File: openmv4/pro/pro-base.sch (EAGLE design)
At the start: 172 parts, among them J2 SAMTEC_FTSH-105-01-F-DVSAMTEC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, J6 RSP-122811-01, M1 9774030243R, M2 9774030243R, Q1 BSS138, Q2 AO3401, U1 W25Q256JVEIQ_TR, U10 STM32H743IIK6, U11 TEXAS_INSTRUMENTS_BQ24072TRGT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, U12 MICROCHIP_ATECC608A-SSHDA-BMI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, U14 IS42S32800, U2 EMIF06-MSD02N16, U3 ME6211C18M5G, U4 PAM2305AABADJ, U5 LSM6DS3TR-C, U6 MICROCHIP_USB3320C-EZK-TRMICR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, U7 LBEE5KL1DX-TEMP, U9 VL53L5CX, X2 USD-1040310811, X3 DF12-36-DS, X4 S2B-PH-K-S(LF)(SN), Y0 SITIME_SIT1533AI-H4-DCC-32.76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, Y1 DSC1001BI1-024.0000

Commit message: Update pro schematics
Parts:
- added D26: GREEN, SparkFun-LED:LED-GREEN0603
- added JP3, JP4: JUMPER-SMT_2_NC_PASTE_SILK, SparkFun-Jumpers:JUMPER-SMT_2_NC_PASTE_SILK
- added R46: 1.5K, sfe:RESISTOR0402-RES
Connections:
- new net N$1: D26.A, R46.1
- new net N$11: JP4.1, R33.2
- new net N$12: JP3.1, R46.2
- new net N$9: D26.C, U11.!PGOOD!
- net OUT: now also JP3.2, JP4.2; no longer R33.2
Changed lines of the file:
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@@
 <part name="R45" library="sfe" deviceset="RESISTOR" device="0402-RES" value="46.4K"/>
 <part name="J6" library="RSP-122811-01" deviceset="RSP-122811-01" device=""/>
+<part name="R46" library="sfe" deviceset="RESISTOR" device="0402-RES" value="1.5K"/>
+<part name="D26" library="SparkFun-LED" library_urn="urn:adsk.eagle:library:529" deviceset="LED-GREEN" device="0603" package3d_urn="urn:adsk.eagle:package:39354/1" value="GREEN"/>
+<part name="JP3" library="SparkFun-Jumpers" library_urn="urn:adsk.eagle:library:528" deviceset="JUMPER-SMT_2_NC_PASTE" device="_SILK" package3d_urn="urn:adsk.eagle:package:39282/1"/>
+<part name="JP4" library="SparkFun-Jumpers" library_urn="urn:adsk.eagle:library:528" deviceset="JUMPER-SMT_2_NC_PASTE" device="_SILK" package3d_urn="urn:adsk.eagle:package:39282/1"/>
 </parts>
 <sheets>
@@
 <text x="96.52" y="391.16" size="1.27" layer="150" font="vector" ratio="20">* Swapped to make
   layout easier</text>
-<text x="134.62" y="358.14" size="7.62" layer="94" font="vector" ratio="20">Battery Charging</text>
+<text x="134.62" y="360.68" size="7.62" layer="94" font="vector" ratio="20">Battery Charging</text>
 <wire x1="132.08" y1="370.84" x2="271.78" y2="370.84" width="0.1524" layer="94" style="longdash"/>
 <text x="134.62" y="419.1" size="7.62" layer="94" font="vector" ratio="20">Power</text>
@@
 <attribute name="VALUE" x="407.924" y="92.202" size="1.778" layer="96" rot="MR0"/>
 </instance>
+<instance part="R46" gate="G$1" x="165.1" y="355.6" smashed="yes">
+<attribute name="NAME" x="161.29" y="357.0986" size="1.778" layer="95"/>
+<attribute name="VALUE" x="161.29" y="352.298" size="1.778" layer="96"/>
+</instance>
+<instance part="D26" gate="G$1" x="154.94" y="355.6" smashed="yes" rot="R270">
+<attribute name="NAME" x="150.368" y="359.029" size="1.778" layer="95" font="vector"/>
+<attribute name="VALUE" x="150.368" y="353.695" size="1.778" layer="96" font="vector" align="top-left"/>
+</instance>
+<instance part="JP3" gate="G$1" x="177.8" y="355.6" smashed="yes">
+<attribute name="NAME" x="175.26" y="358.14" size="1.778" layer="95" font="vector"/>
+<attribute name="VALUE" x="180.34" y="360.68" size="1.778" layer="96" font="vector" align="top-left"/>
+</instance>
+<instance part="JP4" gate="G$1" x="177.8" y="350.52" smashed="yes">
+<attribute name="NAME" x="175.26" y="353.06" size="1.778" layer="95" font="vector"/>
+<attribute name="VALUE" x="180.34" y="355.6" size="1.778" layer="96" font="vector" align="top-left"/>
+</instance>
 </instances>
 <busses>
@@
 <wire x1="193.04" y1="337.82" x2="215.9" y2="337.82" width="0.1524" layer="91"/>
 <junction x="193.04" y="337.82"/>
-<wire x1="193.04" y1="350.52" x2="193.04" y2="345.44" width="0.1524" layer="91"/>
 <pinref part="C4" gate="G$1" pin="2"/>
 <wire x1="193.04" y1="345.44" x2="193.04" y2="337.82" width="0.1524" layer="91"/>
 <wire x1="215.9" y1="337.82" x2="241.3" y2="337.82" width="0.1524" layer="91"/>
 <junction x="215.9" y="337.82"/>
-<pinref part="R33" gate="G$1" pin="2"/>
-<wire x1="193.04" y1="350.52" x2="170.18" y2="350.52" width="0.1524" layer="91"/>
 <pinref part="U11" gate="G$0" pin="EN2"/>
 <wire x1="165.1" y1="322.58" x2="162.56" y2="322.58" width="0.1524" layer="91"/>
@@
 <wire x1="162.56" y1="345.44" x2="193.04" y2="345.44" width="0.1524" layer="91"/>
 <junction x="193.04" y="345.44"/>
+<wire x1="193.04" y1="355.6" x2="193.04" y2="350.52" width="0.1524" layer="91"/>
+<pinref part="JP3" gate="G$1" pin="2"/>
+<wire x1="193.04" y1="350.52" x2="193.04" y2="345.44" width="0.1524" layer="91"/>
+<wire x1="182.88" y1="355.6" x2="193.04" y2="355.6" width="0.1524" layer="91"/>
+<pinref part="JP4" gate="G$1" pin="2"/>
+<wire x1="182.88" y1="350.52" x2="193.04" y2="350.52" width="0.1524" layer="91"/>
+<junction x="193.04" y="350.52"/>
 </segment>
 </net>
@@
 </segment>
 </net>
+<net name="N$1" class="0">
+<segment>
+<pinref part="D26" gate="G$1" pin="A"/>
+<pinref part="R46" gate="G$1" pin="1"/>
+<wire x1="157.48" y1="355.6" x2="160.02" y2="355.6" width="0.1524" layer="91"/>
+</segment>
+</net>
+<net name="N$9" class="0">
+<segment>
+<pinref part="D26" gate="G$1" pin="C"/>
+<wire x1="149.86" y1="355.6" x2="142.24" y2="355.6" width="0.1524" layer="91"/>
+<wire x1="142.24" y1="355.6" x2="142.24" y2="307.34" width="0.1524" layer="91"/>
+<pinref part="U11" gate="G$0" pin="!PGOOD!"/>
+<wire x1="142.24" y1="307.34" x2="165.1" y2="307.34" width="0.1524" layer="91"/>
+</segment>
+</net>
+<net name="N$11" class="0">
+<segment>
+<pinref part="R33" gate="G$1" pin="2"/>
+<pinref part="JP4" gate="G$1" pin="1"/>
+<wire x1="170.18" y1="350.52" x2="172.72" y2="350.52" width="0.1524" layer="91"/>
+</segment>
+</net>
+<net name="N$12" class="0">
+<segment>
+<pinref part="R46" gate="G$1" pin="2"/>
+<pinref part="JP3" gate="G$1" pin="1"/>
+<wire x1="170.18" y1="355.6" x2="172.72" y2="355.6" width="0.1524" layer="91"/>
+</segment>
+</net>

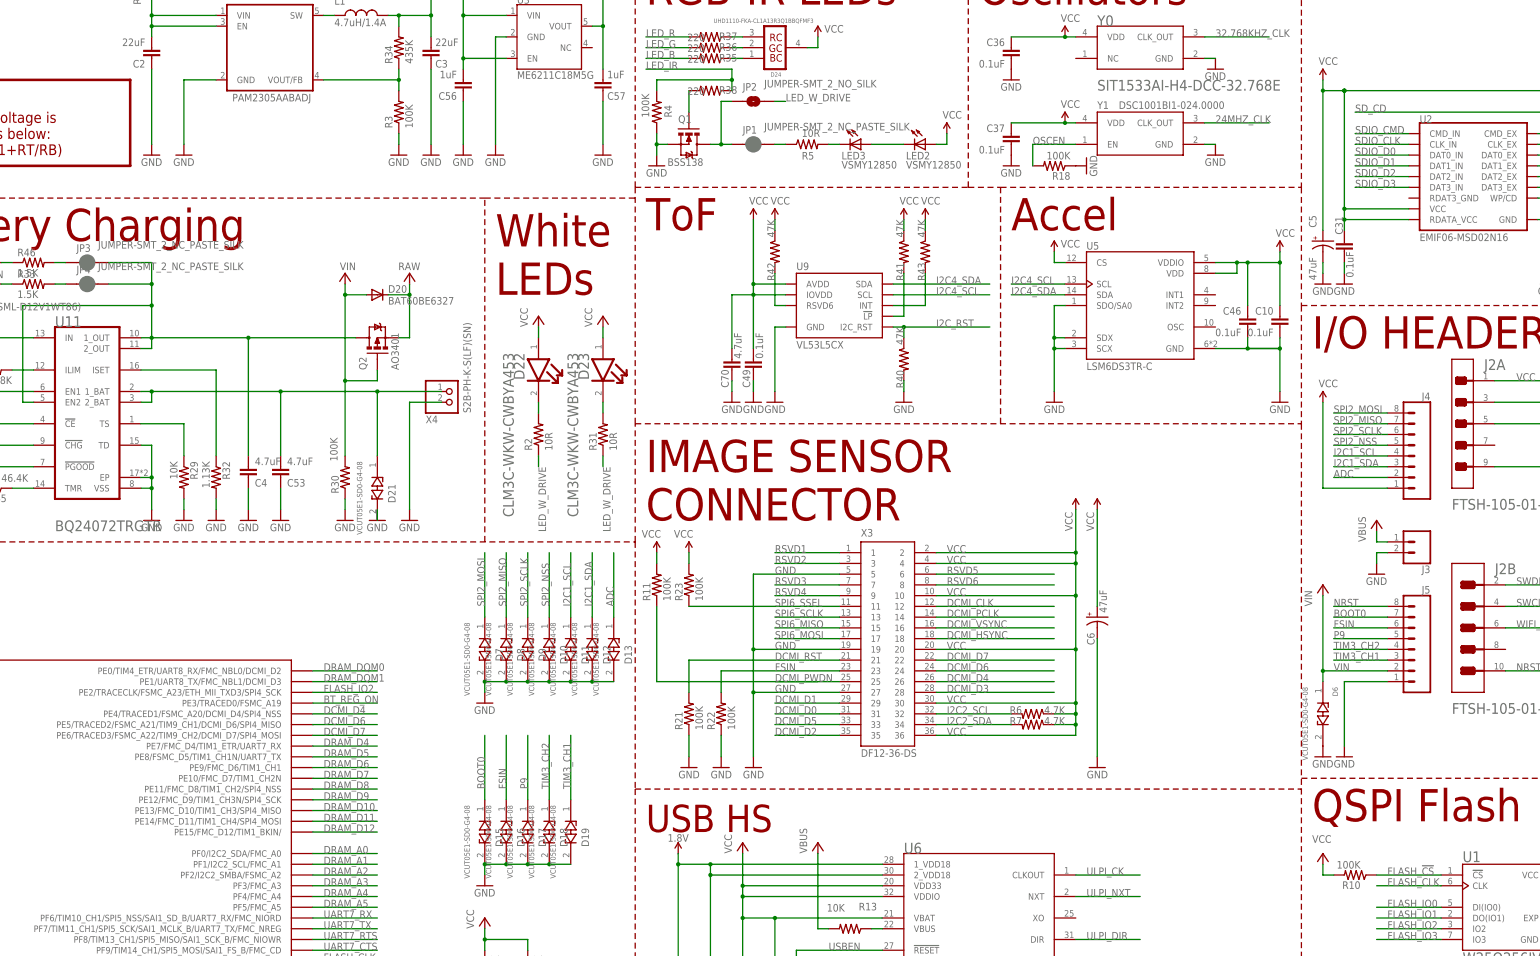
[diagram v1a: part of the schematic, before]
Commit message: Update jumpers to 0 ohm
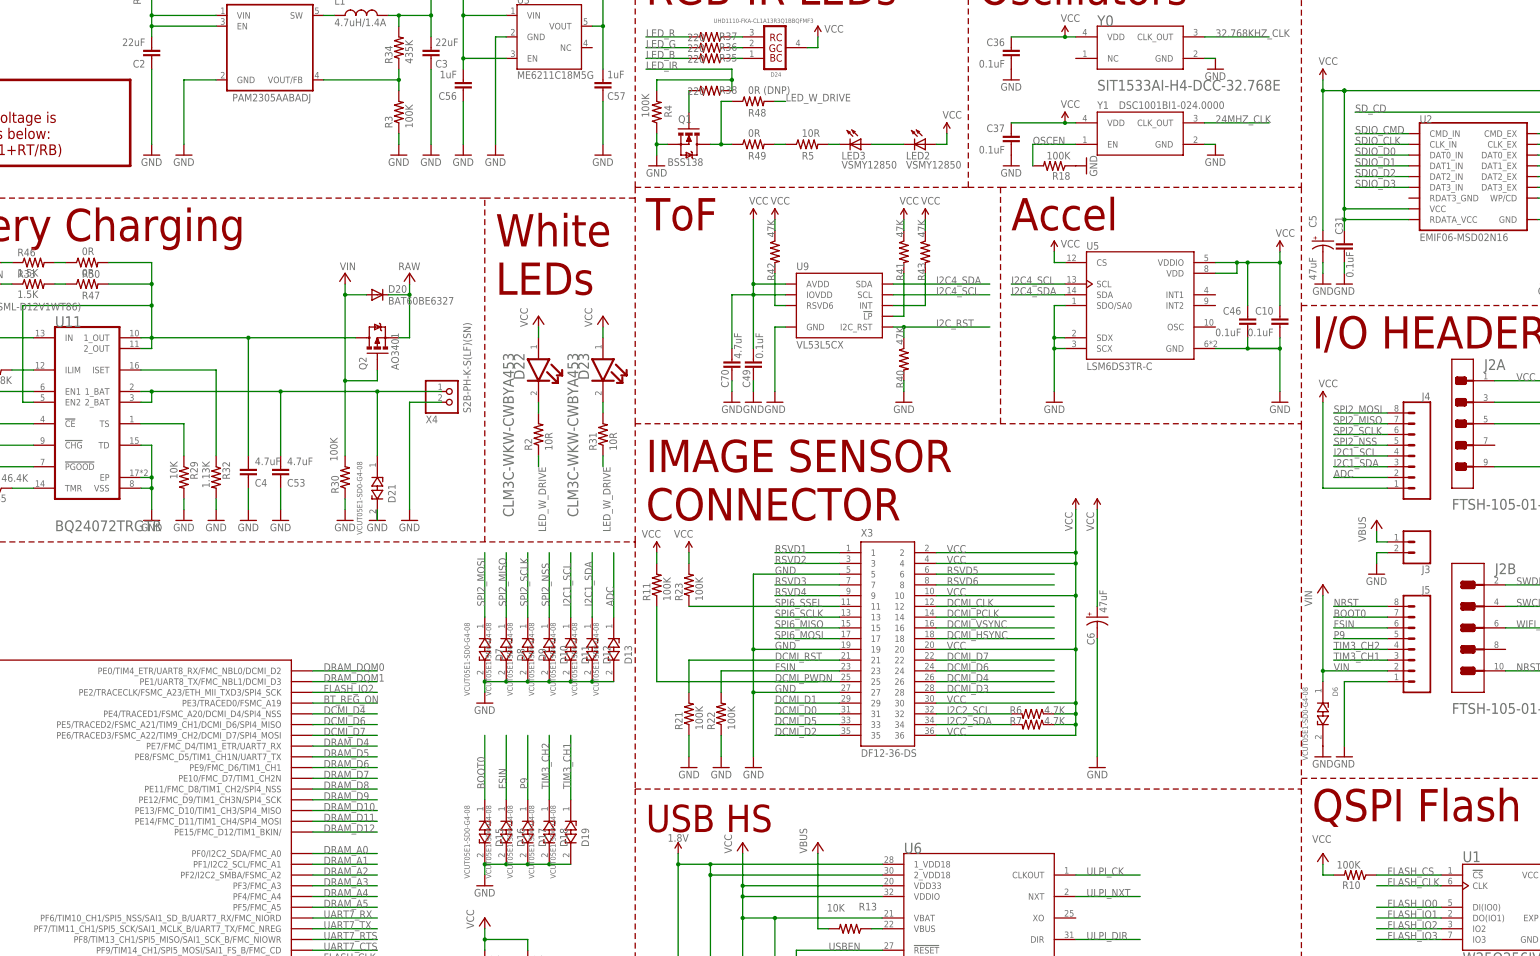
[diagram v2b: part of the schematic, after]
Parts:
- removed JP1, JP3, JP4: JUMPER-SMT_2_NC_PASTE_SILK, SparkFun-Jumpers:JUMPER-SMT_2_NC_PASTE_SILK
- removed JP2: JUMPER-SMT_2_NO_SILK, SparkFun-Jumpers:JUMPER-SMT_2_NO_SILK
- added R47, R49, R50: 0R, sfe:RESISTOR0402-RES
- added R48: 0R (DNP), sfe:RESISTOR0402-RES
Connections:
- removed net FLASH_!CS: R10.1, U1.!CS
- net FLASH_CS: now also R10.1, U1.!CS
- net LED_DRAIN: now also R48.1, R49.1; no longer JP1.1, JP2.1
- net LED_IR_DRIVE: now also R49.2; no longer JP1.2
- net LED_W_DRIVE: now also R48.2; no longer JP2.2
- net N$11: now also R47.1; no longer JP4.1
- net N$12: now also R50.1; no longer JP3.1
- net OUT: now also R47.2, R50.2; no longer JP3.2, JP4.2
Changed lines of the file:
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@@
 <part name="R2" library="sfe" deviceset="RESISTOR" device="0402-RES" value="10R"/>
 <part name="R31" library="sfe" deviceset="RESISTOR" device="0402-RES" value="10R"/>
-<part name="JP1" library="SparkFun-Jumpers" library_urn="urn:adsk.eagle:library:528" deviceset="JUMPER-SMT_2_NC_PASTE" device="_SILK" package3d_urn="urn:adsk.eagle:package:39282/1"/>
-<part name="JP2" library="SparkFun-Jumpers" library_urn="urn:adsk.eagle:library:528" deviceset="JUMPER-SMT_2_NO" device="_SILK" package3d_urn="urn:adsk.eagle:package:39279/1"/>
 <part name="R35" library="sfe" deviceset="RESISTOR" device="0402-RES" value="220"/>
 <part name="R36" library="sfe" deviceset="RESISTOR" device="0402-RES" value="220"/>
@@
 <part name="R46" library="sfe" deviceset="RESISTOR" device="0402-RES" value="1.5K"/>
 <part name="D26" library="SparkFun-LED" library_urn="urn:adsk.eagle:library:529" deviceset="LED-GREEN" device="0603" package3d_urn="urn:adsk.eagle:package:39354/1" value="GREEN"/>
-<part name="JP3" library="SparkFun-Jumpers" library_urn="urn:adsk.eagle:library:528" deviceset="JUMPER-SMT_2_NC_PASTE" device="_SILK" package3d_urn="urn:adsk.eagle:package:39282/1"/>
-<part name="JP4" library="SparkFun-Jumpers" library_urn="urn:adsk.eagle:library:528" deviceset="JUMPER-SMT_2_NC_PASTE" device="_SILK" package3d_urn="urn:adsk.eagle:package:39282/1"/>
+<part name="R47" library="sfe" deviceset="RESISTOR" device="0402-RES" value="0R"/>
+<part name="R48" library="sfe" deviceset="RESISTOR" device="0402-RES" value="0R (DNP)"/>
+<part name="R49" library="sfe" deviceset="RESISTOR" device="0402-RES" value="0R"/>
+<part name="R50" library="sfe" deviceset="RESISTOR" device="0402-RES" value="0R"/>
 </parts>
 <sheets>
@@
 <attribute name="VALUE" x="303.022" y="311.15" size="1.778" layer="96" rot="R90"/>
 </instance>
-<instance part="JP1" gate="G$1" x="335.28" y="383.54" smashed="yes">
-<attribute name="NAME" x="332.74" y="386.08" size="1.778" layer="95" font="vector"/>
-<attribute name="VALUE" x="337.82" y="388.62" size="1.778" layer="96" font="vector" align="top-left"/>
-</instance>
-<instance part="JP2" gate="G$1" x="335.28" y="393.7" smashed="yes">
-<attribute name="NAME" x="332.74" y="396.24" size="1.778" layer="95" font="vector"/>
-<attribute name="VALUE" x="337.82" y="398.78" size="1.778" layer="96" font="vector" align="top-left"/>
-</instance>
 <instance part="R35" gate="G$1" x="325.12" y="403.86" smashed="yes" rot="R180">
 <attribute name="NAME" x="331.47" y="404.9014" size="1.778" layer="95" rot="R180"/>
@@
 <attribute name="VALUE" x="150.368" y="353.695" size="1.778" layer="96" font="vector" align="top-left"/>
 </instance>
-<instance part="JP3" gate="G$1" x="177.8" y="355.6" smashed="yes">
-<attribute name="NAME" x="175.26" y="358.14" size="1.778" layer="95" font="vector"/>
-<attribute name="VALUE" x="180.34" y="360.68" size="1.778" layer="96" font="vector" align="top-left"/>
-</instance>
-<instance part="JP4" gate="G$1" x="177.8" y="350.52" smashed="yes">
-<attribute name="NAME" x="175.26" y="353.06" size="1.778" layer="95" font="vector"/>
-<attribute name="VALUE" x="180.34" y="355.6" size="1.778" layer="96" font="vector" align="top-left"/>
+<instance part="R47" gate="G$1" x="177.8" y="350.52" smashed="yes">
+<attribute name="NAME" x="176.53" y="346.9386" size="1.778" layer="95"/>
+<attribute name="VALUE" x="176.53" y="352.298" size="1.778" layer="96"/>
+</instance>
+<instance part="R48" gate="G$1" x="335.28" y="393.7" smashed="yes">
+<attribute name="NAME" x="334.01" y="390.1186" size="1.778" layer="95"/>
+<attribute name="VALUE" x="334.01" y="395.478" size="1.778" layer="96"/>
+</instance>
+<instance part="R49" gate="G$1" x="335.28" y="383.54" smashed="yes">
+<attribute name="NAME" x="334.01" y="379.9586" size="1.778" layer="95"/>
+<attribute name="VALUE" x="334.01" y="385.318" size="1.778" layer="96"/>
+</instance>
+<instance part="R50" gate="G$1" x="177.8" y="355.6" smashed="yes">
+<attribute name="NAME" x="176.53" y="352.0186" size="1.778" layer="95"/>
+<attribute name="VALUE" x="176.53" y="357.378" size="1.778" layer="96"/>
 </instance>
 </instances>
@@
 </segment>
 </net>
-<net name="FLASH_!CS" class="0">
-<segment>
-<pinref part="U1" gate="G$1" pin="!CS"/>
-<label x="485.14" y="210.82" size="1.778" layer="95"/>
-<pinref part="R10" gate="G$1" pin="1"/>
-<wire x1="482.6" y1="210.82" x2="497.84" y2="210.82" width="0.1524" layer="91"/>
-</segment>
-</net>
 <net name="DAT0" class="0">
 <segment>
@@
 <label x="233.68" y="157.48" size="1.778" layer="95"/>
 </segment>
+<segment>
+<pinref part="U1" gate="G$1" pin="!CS"/>
+<label x="485.14" y="210.82" size="1.778" layer="95"/>
+<pinref part="R10" gate="G$1" pin="1"/>
+<wire x1="482.6" y1="210.82" x2="497.84" y2="210.82" width="0.1524" layer="91"/>
+</segment>
 </net>
 <net name="SPI6_SSEL" class="0">
@@
 <junction x="193.04" y="345.44"/>
 <wire x1="193.04" y1="355.6" x2="193.04" y2="350.52" width="0.1524" layer="91"/>
-<pinref part="JP3" gate="G$1" pin="2"/>
 <wire x1="193.04" y1="350.52" x2="193.04" y2="345.44" width="0.1524" layer="91"/>
 <wire x1="182.88" y1="355.6" x2="193.04" y2="355.6" width="0.1524" layer="91"/>
-<pinref part="JP4" gate="G$1" pin="2"/>
 <wire x1="182.88" y1="350.52" x2="193.04" y2="350.52" width="0.1524" layer="91"/>
 <junction x="193.04" y="350.52"/>
+<pinref part="R47" gate="G$1" pin="2"/>
+<pinref part="R50" gate="G$1" pin="2"/>
 </segment>
 </net>
@@
 </segment>
 <segment>
-<pinref part="JP2" gate="G$1" pin="2"/>
 <wire x1="340.36" y1="393.7" x2="342.9" y2="393.7" width="0.1524" layer="91"/>
 <label x="342.9" y="393.7" size="1.778" layer="95"/>
+<pinref part="R48" gate="G$1" pin="2"/>
 </segment>
 </net>
@@
 <segment>
 <pinref part="Q1" gate="G$1" pin="D"/>
-<pinref part="JP1" gate="G$1" pin="1"/>
 <wire x1="325.12" y1="383.54" x2="327.66" y2="383.54" width="0.1524" layer="91"/>
 <wire x1="327.66" y1="383.54" x2="330.2" y2="383.54" width="0.1524" layer="91"/>
 <wire x1="327.66" y1="383.54" x2="327.66" y2="393.7" width="0.1524" layer="91"/>
 <junction x="327.66" y="383.54"/>
-<pinref part="JP2" gate="G$1" pin="1"/>
 <wire x1="327.66" y1="393.7" x2="330.2" y2="393.7" width="0.1524" layer="91"/>
+<pinref part="R48" gate="G$1" pin="1"/>
+<pinref part="R49" gate="G$1" pin="1"/>
 </segment>
 </net>
 <net name="LED_IR_DRIVE" class="0">
 <segment>
-<pinref part="JP1" gate="G$1" pin="2"/>
 <pinref part="R5" gate="G$1" pin="1"/>
 <wire x1="340.36" y1="383.54" x2="342.9" y2="383.54" width="0.1524" layer="91"/>
+<pinref part="R49" gate="G$1" pin="2"/>
 </segment>
 </net>
@@
 <segment>
 <pinref part="R33" gate="G$1" pin="2"/>
-<pinref part="JP4" gate="G$1" pin="1"/>
 <wire x1="170.18" y1="350.52" x2="172.72" y2="350.52" width="0.1524" layer="91"/>
+<pinref part="R47" gate="G$1" pin="1"/>
 </segment>
 </net>
@@
 <segment>
 <pinref part="R46" gate="G$1" pin="2"/>
-<pinref part="JP3" gate="G$1" pin="1"/>
 <wire x1="170.18" y1="355.6" x2="172.72" y2="355.6" width="0.1524" layer="91"/>
+<pinref part="R50" gate="G$1" pin="1"/>
 </segment>
 </net>
